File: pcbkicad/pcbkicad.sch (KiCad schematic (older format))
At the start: 12 parts, among them U1 STM32F072C8Tx

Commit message: Replaced with a ChibiOS suppported mcu
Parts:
- removed U1: STM32F072C8Tx, Package_QFP:LQFP-48_7x7mm_P0.5mm, symbol MCU_ST_STM32F0:STM32F072C8Tx
- added SW?: SW_Push, symbol Switch:SW_Push
- added U?: STM32F072CBTx, Package_QFP:LQFP-48_7x7mm_P0.5mm, symbol MCU_ST_STM32F0:STM32F072CBTx
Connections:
- wire segments 46 -> 48
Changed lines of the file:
@@
 $EndDescr
-$Comp
-L MCU_ST_STM32F0:STM32F072C8Tx U1
-U 1 1 5FBF2E8D
-P 5250 3550
-F 0 "U1" H 5900 1900 50  0000 C CNN
-F 1 "STM32F072C8Tx" H 5900 1800 50  0000 C CNN
-F 2 "Package_QFP:LQFP-48_7x7mm_P0.5mm" H 4650 2150 50  0001 R CNN
-F 3 "http://www.st.com/st-web-ui/static/active/en/resource/technical/document/datasheet/DM00090510.pdf" H 5250 3550 50  0001 C CNN
-	1    5250 3550
-	1    0    0    -1
-$EndComp
 $Comp
 L Regulator_Linear:AMS1117-3.3 U?
@@
 	1    0    0    -1
 $EndComp
+$Comp
+L Switch:SW_Push SW?
+U 1 1 5FC49B27
+P 4350 2250
+F 0 "SW?" H 4350 2535 50  0000 C CNN
+F 1 "SW_Push" H 4350 2444 50  0000 C CNN
+F 2 "" H 4350 2450 50  0001 C CNN
+F 3 "~" H 4350 2450 50  0001 C CNN
+	1    4350 2250
+	1    0    0    -1
+$EndComp
+Wire Wire Line
+	4150 2250 3900 2250
+Wire Wire Line
+	3900 2250 3900 2300
+$Comp
+L power:GND #PWR?
+U 1 1 5FC4DDE7
+P 3900 2300
+F 0 "#PWR?" H 3900 2050 50  0001 C CNN
+F 1 "GND" H 3905 2127 50  0000 C CNN
+F 2 "" H 3900 2300 50  0001 C CNN
+F 3 "" H 3900 2300 50  0001 C CNN
+	1    3900 2300
+	1    0    0    -1
+$EndComp
+$Comp
+L MCU_ST_STM32F0:STM32F072CBTx U?
+U 1 1 5FC50A36
+P 5250 3550
+F 0 "U?" H 5200 1961 50  0000 C CNN
+F 1 "STM32F072CBTx" H 5200 1870 50  0000 C CNN
+F 2 "Package_QFP:LQFP-48_7x7mm_P0.5mm" H 4650 2150 50  0001 R CNN
+F 3 "http://www.st.com/st-web-ui/static/active/en/resource/technical/document/datasheet/DM00090510.pdf" H 5250 3550 50  0001 C CNN
+	1    5250 3550
+	1    0    0    -1
+$EndComp

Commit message: Added crystal
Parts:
- added C? (x2): 12p, symbol Device:C_Small
- added C?: 100n, symbol Device:C
- added C?: 4.7u, symbol Device:C
- added HSE?: 16Mhz, symbol Device:Crystal_GND24
- added R?: 220, symbol Device:R_Small_US
- added R?: 10k, symbol Device:R_Small_US
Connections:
- net +3V3: now also U?.36 (VDDIO2), C?.2
- net GND: now also C?.1, C?.2, C?.2, HSE?.2, HSE?.4, R?.2
- net BOOT0: now reaches U?.44 (BOOT0)
- net BOOT0: now also R?.1
- net HSE_in: now reaches U?.5 (PF0)
- net HSE_in: now also C?.1, HSE?.1
- net HSE_out: now reaches U?.6 (PF1)
- net HSE_out: now also R?.1
- new net: C?.1, HSE?.3, R?.2
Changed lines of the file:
@@
 	1    0    0    -1
 $EndComp
+Text GLabel 4450 2650 0    50   Input ~ 0
+HSE_in
+Wire Wire Line
+	4450 2650 4550 2650
+Text GLabel 4450 2750 0    50   Input ~ 0
+HSE_out
+Wire Wire Line
+	4450 2750 4550 2750
+$Comp
+L power:GND #PWR?
+U 1 1 5FC5F862
+P 7100 2650
+F 0 "#PWR?" H 7100 2400 50  0001 C CNN
+F 1 "GND" H 7105 2477 50  0000 C CNN
+F 2 "" H 7100 2650 50  0001 C CNN
+F 3 "" H 7100 2650 50  0001 C CNN
+	1    7100 2650
+	1    0    0    -1
+$EndComp
+$Comp
+L Device:Crystal_GND24 HSE?
+U 1 1 5FC5C822
+P 7100 2350
+F 0 "HSE?" H 6700 2600 50  0000 L CNN
+F 1 "16Mhz" H 6700 2500 50  0000 L CNN
+F 2 "" H 7100 2350 50  0001 C CNN
+F 3 "~" H 7100 2350 50  0001 C CNN
+	1    7100 2350
+	1    0    0    -1
+$EndComp
+Text GLabel 6700 2350 0    50   Input ~ 0
+HSE_in
+Wire Wire Line
+	6700 2350 6800 2350
+Text GLabel 8000 2350 2    50   Input ~ 0
+HSE_out
+$Comp
+L Device:R_Small_US R?
+U 1 1 5FC68E56
+P 7750 2350
+F 0 "R?" V 7545 2350 50  0000 C CNN
+F 1 "220" V 7636 2350 50  0000 C CNN
+F 2 "" H 7750 2350 50  0001 C CNN
+F 3 "~" H 7750 2350 50  0001 C CNN
+	1    7750 2350
+	0    1    1    0
+$EndComp
+$Comp
+L Device:C_Small C?
+U 1 1 5FC6A2F6
+P 7450 2550
+F 0 "C?" H 7542 2596 50  0000 L CNN
+F 1 "12p" H 7542 2505 50  0000 L CNN
+F 2 "" H 7450 2550 50  0001 C CNN
+F 3 "~" H 7450 2550 50  0001 C CNN
+	1    7450 2550
+	1    0    0    -1
+$EndComp
+$Comp
+L Device:C_Small C?
+U 1 1 5FC6AE31
+P 6800 2550
+F 0 "C?" H 6600 2500 50  0000 L CNN
+F 1 "12p" H 6500 2400 50  0000 L CNN
+F 2 "" H 6800 2550 50  0001 C CNN
+F 3 "~" H 6800 2550 50  0001 C CNN
+	1    6800 2550
+	1    0    0    -1
+$EndComp
+Wire Wire Line
+	7450 2650 7300 2650
+Wire Wire Line
+	7100 2550 7100 2650
+Connection ~ 7100 2650
+Wire Wire Line
+	6800 2650 7100 2650
+Wire Wire Line
+	6800 2450 6800 2350
+Connection ~ 6800 2350
+Wire Wire Line
+	6800 2350 6950 2350
+Wire Wire Line
+	7450 2450 7450 2350
+Wire Wire Line
+	7450 2350 7250 2350
+Wire Wire Line
+	7450 2350 7650 2350
+Connection ~ 7450 2350
+Wire Wire Line
+	7850 2350 8000 2350
+Wire Wire Line
+	7100 2150 7300 2150
+Wire Wire Line
+	7300 2150 7300 2650
+Connection ~ 7300 2650
+Wire Wire Line
+	7300 2650 7100 2650
+Text GLabel 4450 2450 0    50   Input ~ 0
+BOOT0
+Wire Wire Line
+	4450 2450 4550 2450
+$Comp
+L power:GND #PWR?
+U 1 1 5FC7C779
+P 6450 3550
+F 0 "#PWR?" H 6450 3300 50  0001 C CNN
+F 1 "GND" H 6455 3377 50  0000 C CNN
+F 2 "" H 6450 3550 50  0001 C CNN
+F 3 "" H 6450 3550 50  0001 C CNN
+	1    6450 3550
+	1    0    0    -1
+$EndComp
+$Comp
+L Device:R_Small_US R?
+U 1 1 5FC7DCB6
+P 6450 3450
+F 0 "R?" H 6518 3496 50  0000 L CNN
+F 1 "10k" H 6518 3405 50  0000 L CNN
+F 2 "" H 6450 3450 50  0001 C CNN
+F 3 "~" H 6450 3450 50  0001 C CNN
+	1    6450 3450
+	1    0    0    -1
+$EndComp
+Text GLabel 6450 3350 1    50   Input ~ 0
+BOOT0
+Wire Wire Line
+	5250 1900 5450 1900
+Wire Wire Line
+	5450 1900 5450 2050
+Connection ~ 5250 1900
+$Comp
+L Device:C C?
+U 1 1 5FC84E72
+P 850 3200
+F 0 "C?" H 735 3154 50  0000 R CNN
+F 1 "100n" H 735 3245 50  0000 R CNN
+F 2 "" H 888 3050 50  0001 C CNN
+F 3 "~" H 850 3200 50  0001 C CNN
+	1    850  3200
+	1    0    0    1
+$EndComp
+$Comp
+L Device:C C?
+U 1 1 5FC855A9
+P 3650 3200
+F 0 "C?" H 3535 3154 50  0000 R CNN
+F 1 "4.7u" H 3535 3245 50  0000 R CNN
+F 2 "" H 3688 3050 50  0001 C CNN
+F 3 "~" H 3650 3200 50  0001 C CNN
+	1    3650 3200
+	1    0    0    1
+$EndComp
+Wire Wire Line
+	3650 3050 3650 2950
+Wire Wire Line
+	3650 2950 3200 2950
+Connection ~ 3200 2950
+Wire Wire Line
+	3650 3350 3650 3500
+Wire Wire Line
+	3650 3500 3200 3500
 $EndSCHEMATC

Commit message: Finsished rough draft of schematic
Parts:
- added J?: USBDaughterboard, symbol Connector_Generic:Conn_01x04
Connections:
- net +3V3: now also C?.2
- net GND: now also C?.1, J?.4 (Pin_4)
- net VCC: now also J?.1 (Pin_1)
- net D-: now reaches U?.32 (PA11)
- net D-: now also J?.2 (Pin_2)
- net D+: now reaches U?.33 (PA12)
- net D+: now also J?.3 (Pin_3)
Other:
- note added: "11/26/2020"
- note added: "CSMACRO"
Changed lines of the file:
@@
 Wire Wire Line
 	3650 3500 3200 3500
+Text GLabel 6100 4450 2    50   Input ~ 0
+D-
+Text GLabel 6100 4550 2    50   Input ~ 0
+D+
+Wire Wire Line
+	6100 4550 5850 4550
+Wire Wire Line
+	6100 4450 5850 4450
+Text Notes 7350 7500 0    50   ~ 0
+CSMACRO
+Text Notes 8150 7650 0    50   ~ 0
+11/26/2020
+Wire Wire Line
+	1000 2950 850  2950
+Wire Wire Line
+	850  2950 850  3050
+Connection ~ 1000 2950
+Wire Wire Line
+	850  3350 850  3500
+Wire Wire Line
+	850  3500 1350 3500
+Connection ~ 1350 3500
+$Comp
+L Connector_Generic:Conn_01x04 J?
+U 1 1 5FC96AD3
+P 8950 3400
+F 0 "J?" H 9030 3392 50  0000 L CNN
+F 1 "USBDaughterboard" H 9030 3301 50  0000 L CNN
+F 2 "" H 8950 3400 50  0001 C CNN
+F 3 "~" H 8950 3400 50  0001 C CNN
+	1    8950 3400
+	1    0    0    -1
+$EndComp
+Wire Wire Line
+	8750 3300 8600 3300
+Wire Wire Line
+	8600 3300 8600 3200
+$Comp
+L power:VCC #PWR?
+U 1 1 5FC9F18A
+P 8600 3200
+F 0 "#PWR?" H 8600 3050 50  0001 C CNN
+F 1 "VCC" H 8615 3373 50  0000 C CNN
+F 2 "" H 8600 3200 50  0001 C CNN
+F 3 "" H 8600 3200 50  0001 C CNN
+	1    8600 3200
+	1    0    0    -1
+$EndComp
+$Comp
+L power:GND #PWR?
+U 1 1 5FCA0124
+P 8600 3700
+F 0 "#PWR?" H 8600 3450 50  0001 C CNN
+F 1 "GND" H 8605 3527 50  0000 C CNN
+F 2 "" H 8600 3700 50  0001 C CNN
+F 3 "" H 8600 3700 50  0001 C CNN
+	1    8600 3700
+	1    0    0    -1
+$EndComp
+Wire Wire Line
+	8750 3600 8600 3600
+Wire Wire Line
+	8600 3600 8600 3700
+Text GLabel 8450 3400 0    50   Input ~ 0
+D-
+Text GLabel 8450 3500 0    50   Input ~ 0
+D+
+Wire Wire Line
+	8450 3500 8750 3500
+Wire Wire Line
+	8450 3400 8750 3400
 $EndSCHEMATC

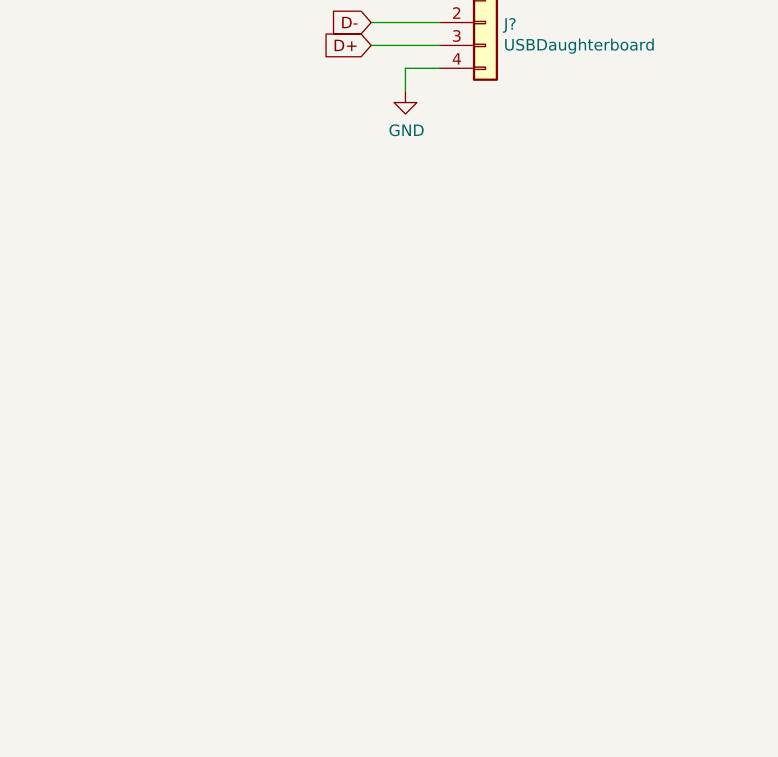
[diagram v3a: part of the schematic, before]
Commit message: Finished keyboard matrix
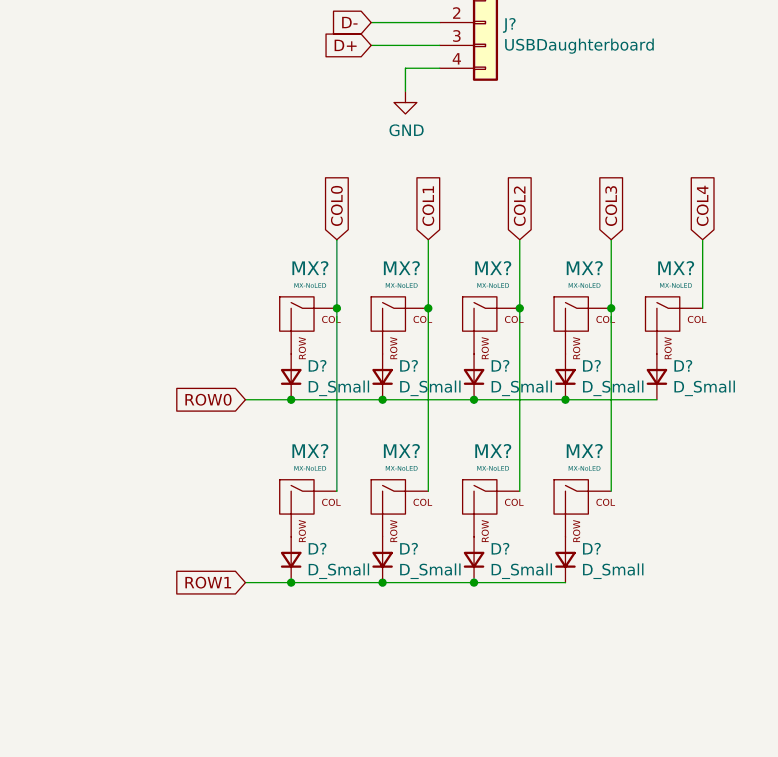
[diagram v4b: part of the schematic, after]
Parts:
- added D? (x9): D_Small, symbol Device:D_Small
- added MX? (x9): MX-NoLED, symbol MX_Alps_Hybrid:MX-NoLED
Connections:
- new net: D?.2 (A), MX?.2 (ROW) (x9)
- new net COL0: MX?.1 (COL), MX?.1 (COL)
- new net COL1: MX?.1 (COL), MX?.1 (COL)
- new net COL2: MX?.1 (COL), MX?.1 (COL)
- new net COL3: MX?.1 (COL), MX?.1 (COL)
- new net COL4: MX?.1 (COL)
- new net ROW0: D?.1 (K), D?.1 (K), D?.1 (K), D?.1 (K), D?.1 (K)
- new net ROW1: D?.1 (K), D?.1 (K), D?.1 (K), D?.1 (K)

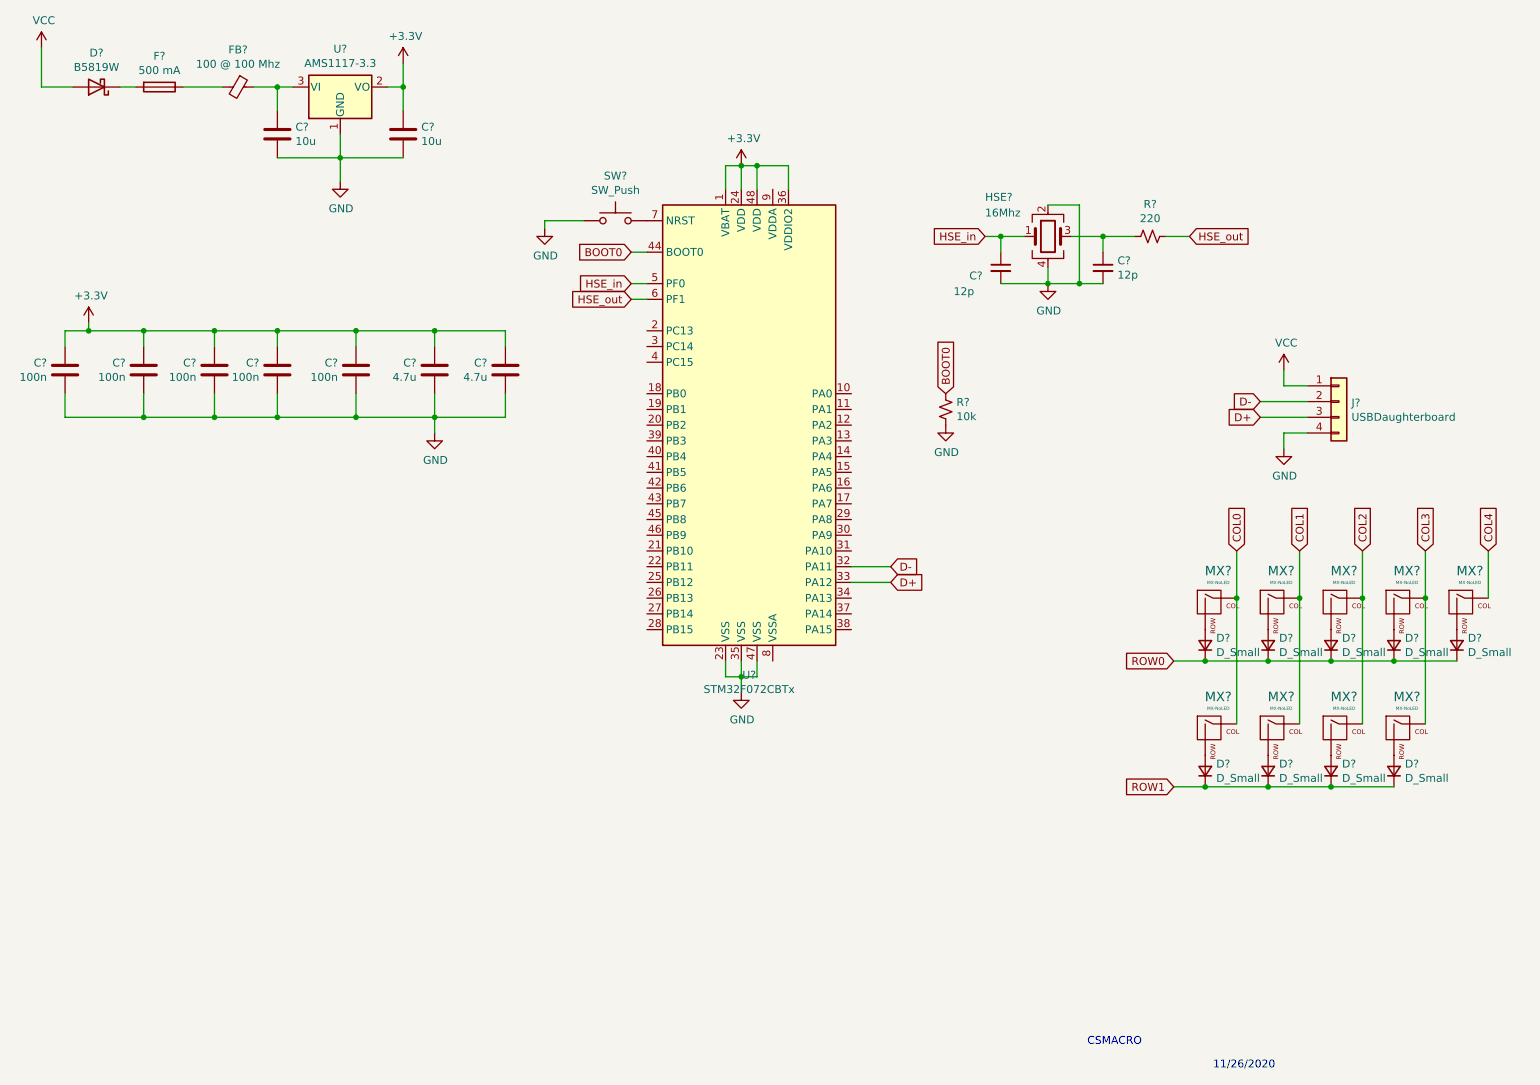
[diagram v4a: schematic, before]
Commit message: Assigned footprints
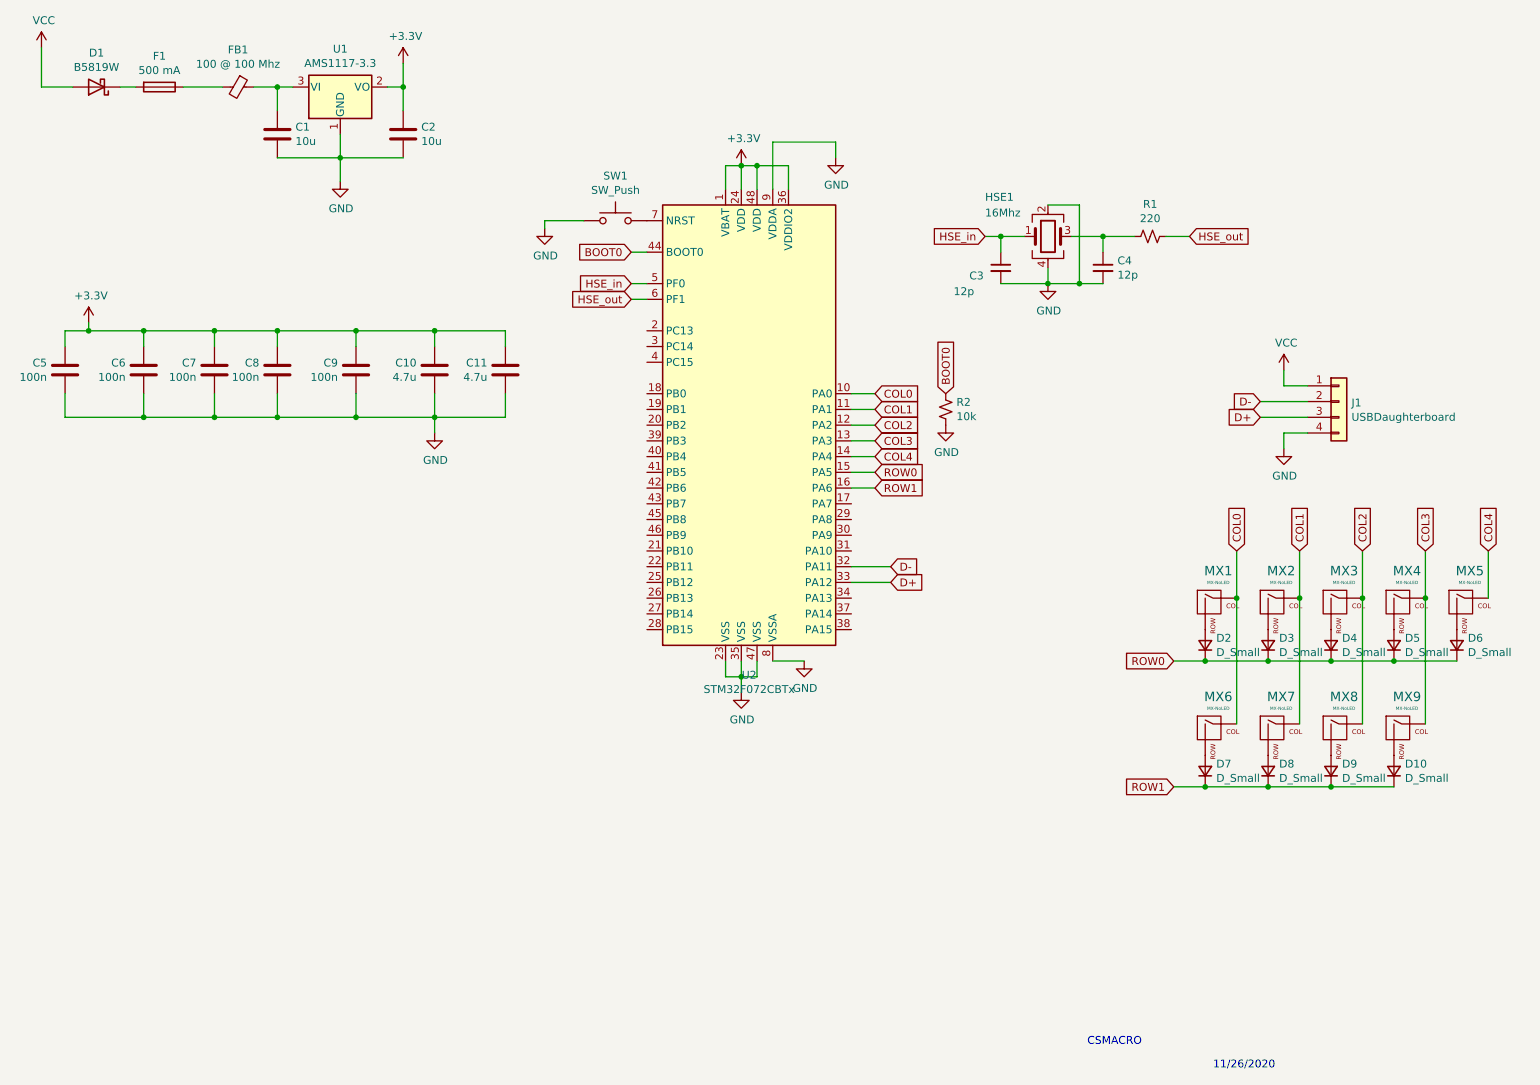
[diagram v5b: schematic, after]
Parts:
- C1, C10, C11, C2, C3, C4, C5, C6, C7, C8, C9: renamed from C?; footprint (none) -> Capacitor_SMD:C_0805_2012Metric
- D1, D10, D2, D3, D4, D5, D6, D7, D8, D9: renamed from D?; footprint (none) -> Diode_SMD:D_SOD-123
- F1: renamed from F?; footprint (none) -> Fuse:Fuse_1206_3216Metric
- FB1: renamed from FB?; footprint (none) -> Ferrite_THT:LairdTech_28C0236-0JW-10
- HSE1: renamed from HSE?; footprint (none) -> Crystal:Crystal_SMD_3225-4Pin_3.2x2.5mm
- J1: renamed from J?; footprint (none) -> random-keyboard-parts:Molex-0548190589
- MX1, MX2, MX3, MX4, MX5, MX6, MX7, MX8, MX9: renamed from MX?; footprint (none) -> Button_Switch_Keyboard:SW_Cherry_MX_1.00u_PCB
- R1, R2: renamed from R?; footprint (none) -> Resistor_SMD:R_0805_2012Metric
- SW1: renamed from SW?; footprint (none) -> Button_Switch_SMD:SW_DIP_SPSTx01_Slide_6.7x4.1mm_W6.73mm_P2.54mm_LowProfile_JPin
- gave numbers to parts that had none: 2
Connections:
- net COL0: now also U2.10 (PA0)
- net COL1: now also U2.11 (PA1)
- net COL2: now also U2.12 (PA2)
- net COL3: now also U2.13 (PA3)
- net COL4: now also U2.14 (PA4)
- net GND: now also U2.8 (VSSA), U2.9 (VDDA)
- net ROW0: now also U2.15 (PA5)
- net ROW1: now also U2.16 (PA6)

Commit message: Finished most of pcb layout
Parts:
- removed SW1: SW_Push, Button_Switch_SMD:SW_DIP_SPSTx01_Slide_6.7x4.1mm_W6.73mm_P2.54mm_LowProfile_JPin, symbol Switch:SW_Push
- C1: footprint Capacitor_SMD:C_0805_2012Metric -> Connector_JST:JST_SH_SM04B-SRSS-TB_1x04-1MP_P1.00mm_Horizontal
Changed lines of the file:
@@
 F 0 "C1" H 2315 1746 50  0000 L CNN
 F 1 "10u" H 2315 1655 50  0000 L CNN
-F 2 "Capacitor_SMD:C_0805_2012Metric" H 2238 1550 50  0001 C CNN
+F 2 "Connector_JST:JST_SH_SM04B-SRSS-TB_1x04-1MP_P1.00mm_Horizontal" H 2238 1550 50  0001 C CNN
 F 3 "~" H 2200 1700 50  0001 C CNN
 	1    2200 1700
@@
 	1    0    0    -1
 $EndComp
-$Comp
-L Switch:SW_Push SW1
-U 1 1 5FC49B27
-P 4350 2250
-F 0 "SW1" H 4350 2535 50  0000 C CNN
-F 1 "SW_Push" H 4350 2444 50  0000 C CNN
-F 2 "Button_Switch_SMD:SW_DIP_SPSTx01_Slide_6.7x4.1mm_W6.73mm_P2.54mm_LowProfile_JPin" H 4350 2450 50  0001 C CNN
-F 3 "~" H 4350 2450 50  0001 C CNN
-	1    4350 2250
-	1    0    0    -1
-$EndComp
-Wire Wire Line
-	4150 2250 3900 2250
-Wire Wire Line
-	3900 2250 3900 2300
-$Comp
-L power:GND #PWR0108
-U 1 1 5FC4DDE7
-P 3900 2300
-F 0 "#PWR0108" H 3900 2050 50  0001 C CNN
-F 1 "GND" H 3905 2127 50  0000 C CNN
-F 2 "" H 3900 2300 50  0001 C CNN
-F 3 "" H 3900 2300 50  0001 C CNN
-	1    3900 2300
-	1    0    0    -1
-$EndComp

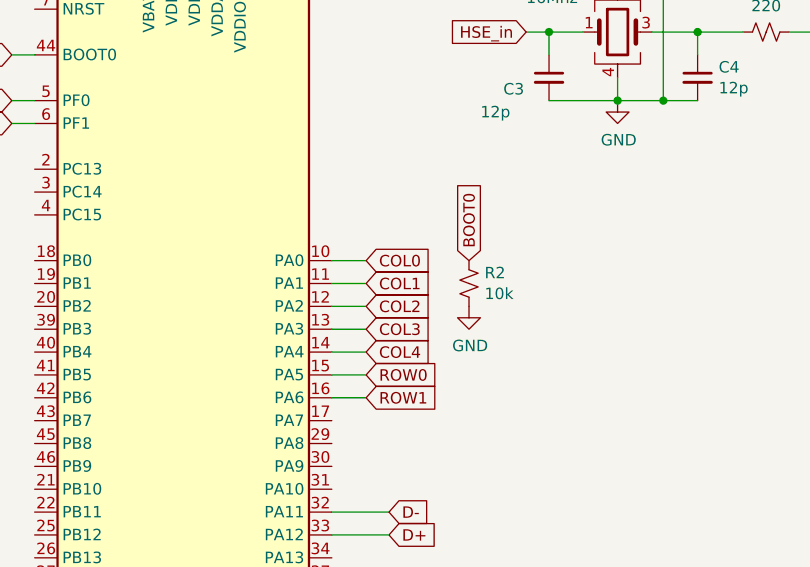
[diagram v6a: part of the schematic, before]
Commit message: First attempt at routing
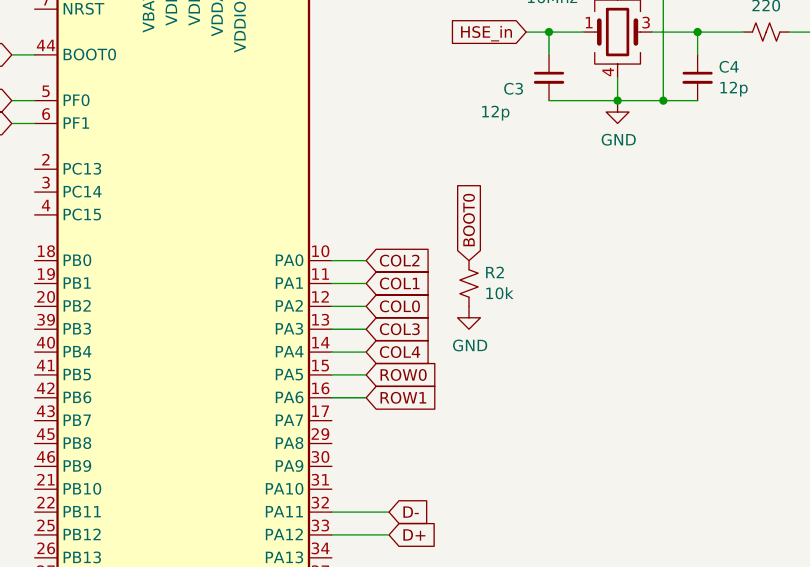
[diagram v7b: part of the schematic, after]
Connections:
- net COL0: now also U2.12 (PA2); no longer U2.10 (PA0)
- net COL2: now also U2.10 (PA0); no longer U2.12 (PA2)
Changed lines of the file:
@@
 	1    0    0    -1
 $EndComp
-Text GLabel 6000 3350 2    50   Input ~ 0
+Text GLabel 6000 3550 2    50   Input ~ 0
 COL0
 Text GLabel 6000 3450 2    50   Input ~ 0
 COL1
-Text GLabel 6000 3550 2    50   Input ~ 0
+Text GLabel 6000 3350 2    50   Input ~ 0
 COL2
 Text GLabel 6000 3650 2    50   Input ~ 0
